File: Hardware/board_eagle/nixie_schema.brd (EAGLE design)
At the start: 150 x 170 mm, 103 parts, among them P1 100k, Q1 BC856B, Q2 IRF740S, U2 MC7940N

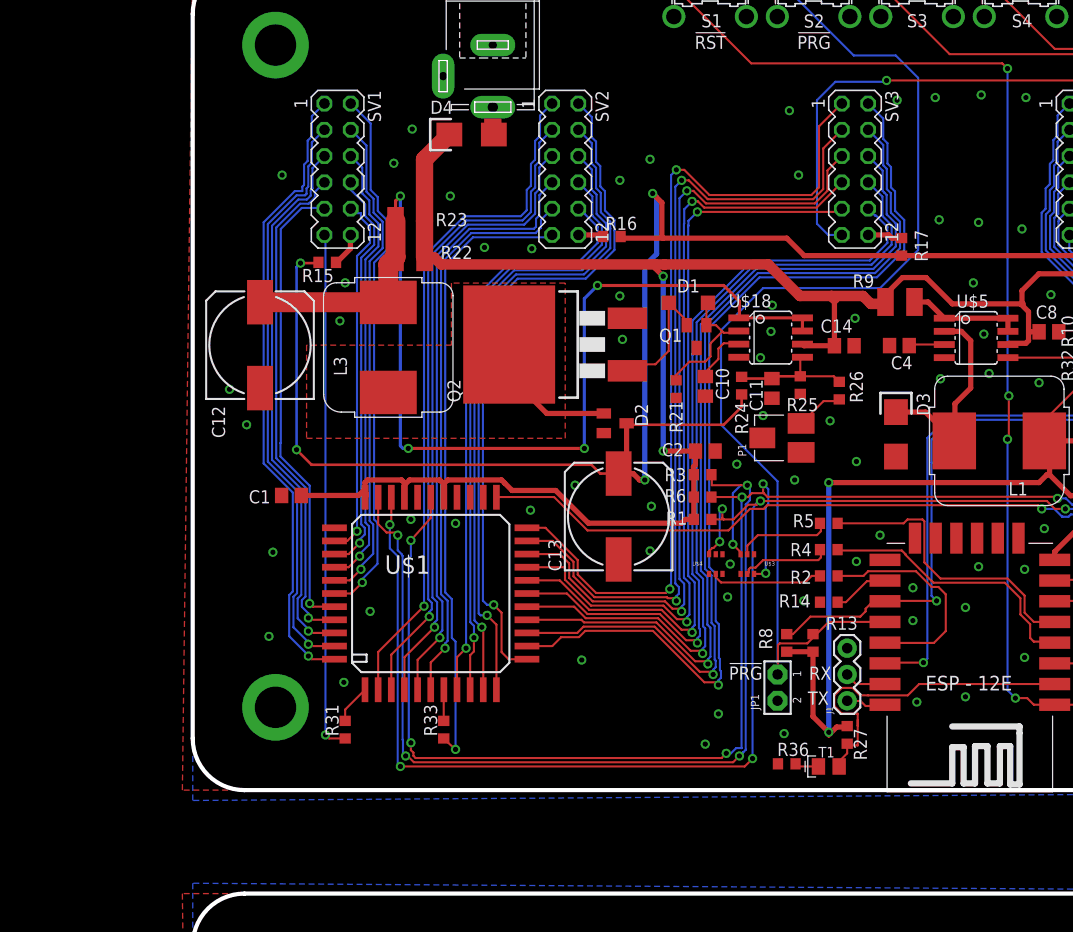
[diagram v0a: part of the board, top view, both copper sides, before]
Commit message: Modified both switching PSUs for the new VFD requirements
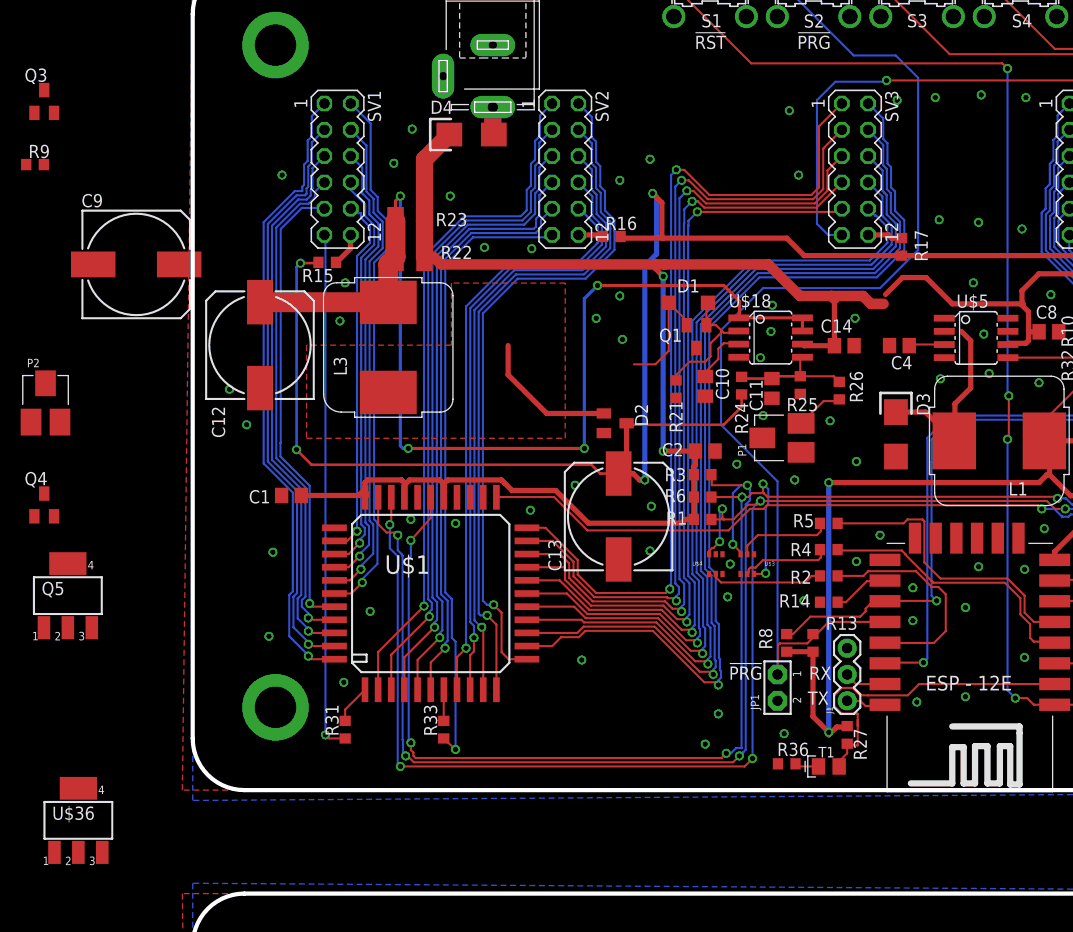
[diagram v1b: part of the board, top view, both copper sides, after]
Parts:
- removed Q2: IRF740S, nixe_cmp:D2PACK
- added C9: 220u, rcl:153CLV-1014
- added P2: 10k, nixe_cmp:UNI_POT_SMD
- added Q3: BC856B, nixe_cmp:SOT23
- added Q4: BCX70H, nixe_cmp:SOT23
- added Q5: NTF5P03, nixe_cmp:SOT223
- added U$36: IPN60R3K4CE_NMOS, nixe_cmp:SOT223
- R9: value 0.5R -> 1k; device eagle-ltspice:R1210 -> resistor:R0603
- moved R9 84.6 mm to (-15.2, 60.5)
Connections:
- new net N$102: Q3.2, Q4.2, Q5.1
- net +3V3: now also P2.P$1
- net GND: now also C9.-, Q3.3, U$36.3, U$5.2; no longer Q2.3
- net N$103: now also P2.P$2
- net N$13: now also Q5.2, Q5.4; no longer U$5.2
- net N$5: now also Q3.1, Q4.1; no longer U$5.7
- net N$95: now also U$36.1; no longer Q2.1
- net VCC: now also C9.+, Q4.3, Q5.3, U$5.7
- net V_PULSE: now also U$36.2, U$36.4; no longer Q2.2
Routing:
- net N$5: track 11.0 -> 0.00 mm
- net N$13: track 19.8 -> 18.2 mm
- net VCC: track 258.9 -> 257.9 mm
- net N$95: track 12.3 -> 11.4 mm

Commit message: Modified IN-14 device to accomodate IV-11 VFD
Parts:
- N1, N2, N3, N4, N5, N6: value IN-14_FIXED -> IN-14_IV-11_COMBI; device russian-nixies:IN-14 -> nixe_cmp:IN-14_IV-11
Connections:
- net N$1: now also N2.RHDP(NC); no longer N2.RHDP
- net N$10: now also N1.A(NC); no longer N1.A
- net N$19: now also N2.A(NC); no longer N2.A
- net N$2: now also N1.6(G); no longer N1.6
- net N$21: now also N3.A(NC); no longer N3.A
- net N$23: now also N2.6(G); no longer N2.6
- net N$24: now also N1.9(D); no longer N1.9
- net N$25: now also N1.1(GRID); no longer N1.1
- net N$26: now also N1.2(C); no longer N1.2
- net N$27: now also N1.3(DP); no longer N1.3
- net N$28: now also N1.4(B); no longer N1.4
- net N$29: now also N1.5(A); no longer N1.5
- net N$30: now also N1.RHDP(NC); no longer N1.RHDP
- net N$31: now also N2.7(F); no longer N2.7
- net N$32: now also N2.8(E); no longer N2.8
- net N$33: now also N2.9(D); no longer N2.9
- net N$34: now also N2.0(CAT); no longer N2.0
- net N$35: now also N3.RHDP(NC); no longer N3.RHDP
- net N$36: no longer N3.6
- net N$37: no longer N3.7
- net N$38: now also N2.5(A); no longer N2.5
- net N$39: now also N2.4(B); no longer N2.4
- net N$40: now also N2.3(DP); no longer N2.3
- net N$41: now also N2.2(C); no longer N2.2
- net N$42: now also N2.1(GRID); no longer N2.1
- net N$43: no longer N3.8
- net N$44: no longer N3.9
- net N$45: now also N6.A(NC); no longer N6.A
- net N$46: no longer N3.0
- net N$47: now also N4.RHDP(NC); no longer N4.RHDP
- net N$48: no longer N4.6
- net N$49: no longer N3.5
- net N$50: no longer N3.4
- net N$51: no longer N3.3
- net N$52: no longer N3.2
- net N$53: no longer N3.1
- net N$54: no longer N4.7
- net N$55: no longer N4.8
- net N$56: no longer N4.9
- net N$57: no longer N4.0
- net N$58: now also N5.RHDP(NC); no longer N5.RHDP
- net N$59: no longer N4.5
- net N$6: now also N1.7(F); no longer N1.7
- net N$60: no longer N4.4
- net N$61: no longer N4.3
- net N$62: no longer N4.2
- net N$63: no longer N4.1
- net N$64: no longer N5.6
- net N$65: no longer N5.7
- net N$66: no longer N5.8
- net N$67: no longer N5.9
- net N$68: no longer N5.0
- net N$69: no longer N5.5
- net N$7: now also N1.8(E); no longer N1.8
- net N$70: no longer N5.4
- net N$71: no longer N5.3
- net N$72: no longer N5.2
- net N$73: no longer N5.1
- net N$75: now also N6.RHDP(NC); no longer N6.RHDP
- net N$76: no longer N6.6
- net N$77: no longer N6.7
- net N$78: no longer N6.8
- net N$79: no longer N6.9
- net N$80: no longer N6.5
- net N$81: no longer N6.4
- net N$82: no longer N6.3
- net N$83: no longer N6.2
- net N$84: no longer N6.1
- net N$86: no longer N6.0
- net N$88: now also N4.A(NC); no longer N4.A
- net N$94: now also N1.0(CAT); no longer N1.0
- net N$98: now also N5.A(NC); no longer N5.A
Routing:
- net N$83: track 20.0 -> 6.89 mm
- net N$79: track 20.0 -> 6.89 mm
- net N$52: track 20.0 -> 6.89 mm
- net N$41: track 20.0 -> 6.89 mm
- net N$33: track 20.0 -> 6.89 mm
- net N$26: track 20.0 -> 6.89 mm
- net N$24: track 20.0 -> 6.89 mm
- net N$72: track 20.0 -> 6.89 mm
- net N$67: track 20.0 -> 6.89 mm
- net N$62: track 20.0 -> 6.89 mm
- net N$56: track 20.0 -> 6.89 mm
- net N$44: track 20.0 -> 6.89 mm
- net N$94: track 14.3 -> 5.37 mm
- net N$68: track 14.3 -> 5.37 mm
- net N$57: track 14.3 -> 5.37 mm
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
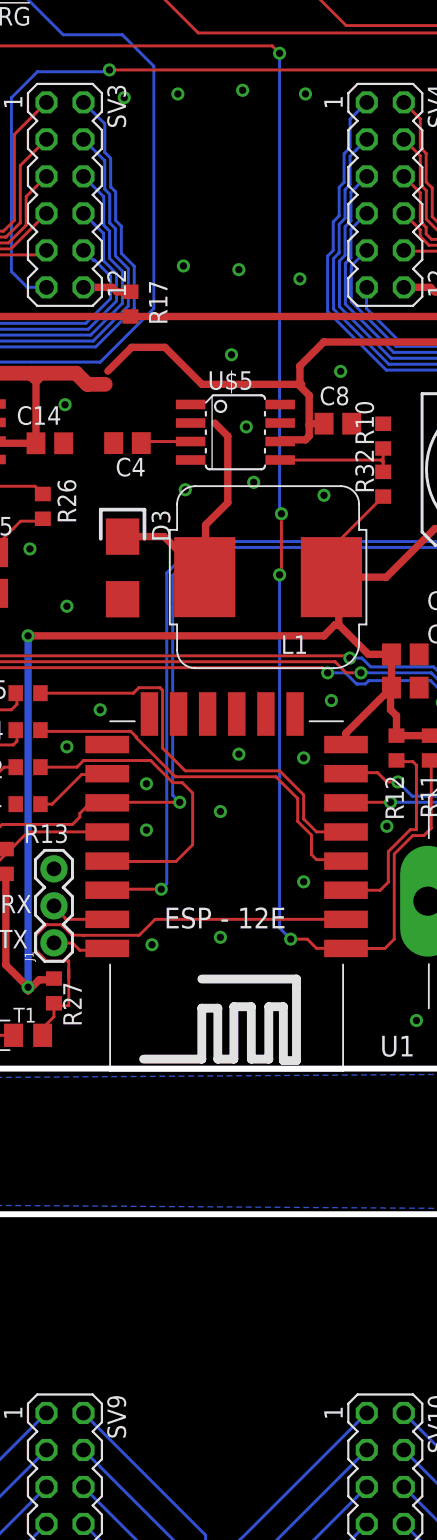
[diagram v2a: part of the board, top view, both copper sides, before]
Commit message: Added Eagle libraries for components. New symbols for Solder bridge and cut trace comps
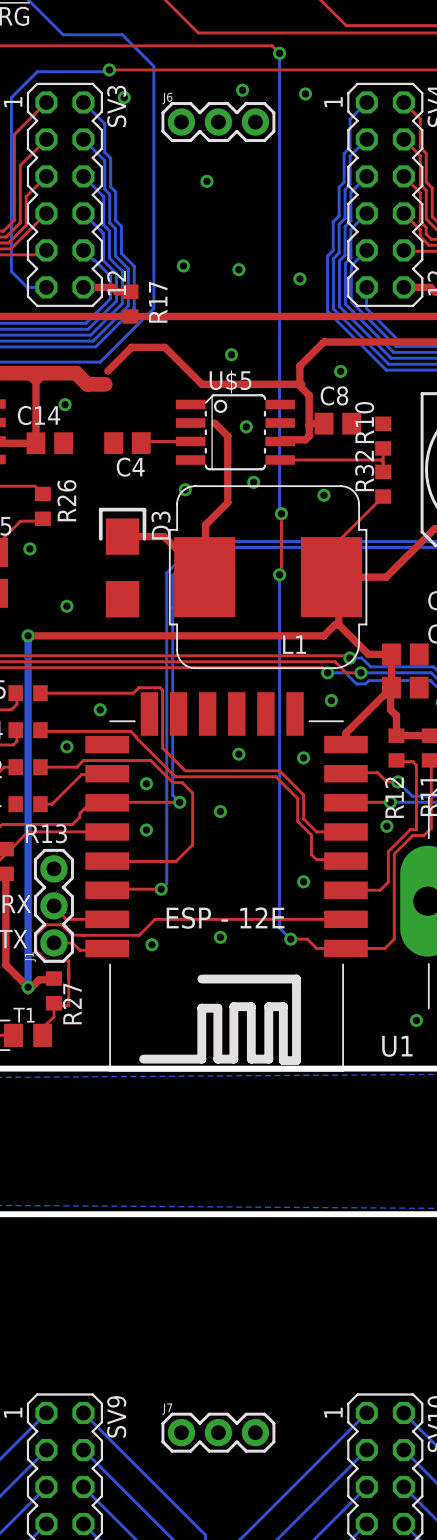
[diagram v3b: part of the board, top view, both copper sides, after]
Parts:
- added J6, J7: (no value), SparkFun-Connectors:1X03
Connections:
- net +3V3: now also J6.2, J7.2
- net GND: now also J6.3, J7.3
- net VCC: now also J6.1, J7.1
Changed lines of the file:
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@@
 <layer number="148" name="DrillLegend_01-20" color="7" fill="1" visible="no" active="yes"/>
 <layer number="149" name="DrillLegend_02-15" color="7" fill="1" visible="no" active="yes"/>
-<layer number="150" name="Notes" color="7" fill="1" visible="no" active="yes"/>
+<layer number="150" name="Notes" color="7" fill="1" visible="yes" active="yes"/>
 <layer number="151" name="HeatSink" color="7" fill="1" visible="no" active="yes"/>
 <layer number="152" name="_bDocu" color="7" fill="1" visible="no" active="yes"/>
@@
 <attribute name="V_DS" value="&gt;220 V" x="-11.049" y="-2.921" size="1.778" layer="27" display="off"/>
 </element>
-<element name="N1" library="nixe_cmp" package="IN-14_IV-11" value="IN-14_IV-11_COMBI" x="14" y="-50" rot="R180"/>
-<element name="N2" library="nixe_cmp" package="IN-14_IV-11" value="IN-14_IV-11_COMBI" x="36" y="-50" rot="R180"/>
-<element name="N3" library="nixe_cmp" package="IN-14_IV-11" value="IN-14_IV-11_COMBI" x="64" y="-50" rot="R180"/>
-<element name="N4" library="nixe_cmp" package="IN-14_IV-11" value="IN-14_IV-11_COMBI" x="86" y="-50" rot="R180"/>
-<element name="N5" library="nixe_cmp" package="IN-14_IV-11" value="IN-14_IV-11_COMBI" x="114" y="-50" rot="R180"/>
-<element name="N6" library="nixe_cmp" package="IN-14_IV-11" value="IN-14_IV-11_COMBI" x="136" y="-50" rot="R180"/>
+<element name="N1" library="nixe_cmp" package="IN-14_IV-11" value="IN-14_IV-11_COMBI" x="14" y="-50" locked="yes" rot="R180"/>
+<element name="N2" library="nixe_cmp" package="IN-14_IV-11" value="IN-14_IV-11_COMBI" x="36" y="-50" locked="yes" rot="R180"/>
+<element name="N3" library="nixe_cmp" package="IN-14_IV-11" value="IN-14_IV-11_COMBI" x="64" y="-50" locked="yes" rot="R180"/>
+<element name="N4" library="nixe_cmp" package="IN-14_IV-11" value="IN-14_IV-11_COMBI" x="86" y="-50" locked="yes" rot="R180"/>
+<element name="N5" library="nixe_cmp" package="IN-14_IV-11" value="IN-14_IV-11_COMBI" x="114" y="-50" locked="yes" rot="R180"/>
+<element name="N6" library="nixe_cmp" package="IN-14_IV-11" value="IN-14_IV-11_COMBI" x="136" y="-50" locked="yes" rot="R180"/>
+<element name="J6" library="SparkFun-Connectors" package="1X03" value="" x="72" y="65" locked="yes"/>
+<element name="J7" library="SparkFun-Connectors" package="1X03" value="" x="72" y="-25" locked="yes"/>
 </elements>
 <signals>
@@
 <contactref element="Q4" pad="3"/>
 <contactref element="Q5" pad="3"/>
-<wire x1="78.8964" y1="43.18" x2="78.7794" y2="44.333" width="0" layer="19" extent="1-1"/>
+<contactref element="J6" pad="1"/>
+<contactref element="J7" pad="1"/>
+<wire x1="70.866" y1="49.53" x2="72" y2="65" width="0" layer="19" extent="1-1"/>
 <wire x1="66.766" y1="46.99" x2="66.948" y2="47.898" width="0" layer="19" extent="1-1"/>
+<wire x1="78.7794" y1="44.333" x2="78.8964" y2="43.18" width="0" layer="19" extent="1-1"/>
 <wire x1="-1.311" y1="50.8" x2="22.4" y2="51.5" width="0" layer="19" extent="1-1"/>
 <wire x1="-16.09" y1="60.452" x2="-1.311" y2="50.8" width="0" layer="19" extent="1-1"/>
 <wire x1="-9.7536" y1="15.6972" x2="10.494" y2="28.474" width="0" layer="19" extent="1-1"/>
 <wire x1="-14.351" y1="28.659" x2="-9.7536" y2="15.6972" width="0" layer="19" extent="1-1"/>
+<wire x1="72" y1="-25" x2="48.426" y2="26.162" width="0" layer="19" extent="1-1"/>
 </signal>
 <signal name="GND">
@@
 <via x="75.946" y="54.864" extent="1-16" drill="0.5"/>
 <via x="76.2" y="67.183" extent="1-16" drill="0.5"/>
-<via x="71.755" y="66.929" extent="1-16" drill="0.5"/>
+<via x="73.755" y="60.929" extent="1-16" drill="0.5"/>
 <via x="80.137" y="54.229" extent="1-16" drill="0.5"/>
 <via x="80.518" y="66.929" extent="1-16" drill="0.5"/>
@@
 <contactref element="Q3" pad="3"/>
 <contactref element="U$36" pad="3"/>
+<contactref element="J6" pad="3"/>
+<contactref element="J7" pad="3"/>
 <wire x1="143.51" y1="53.848" x2="142" y2="72" width="0" layer="19" extent="1-1"/>
 <wire x1="145.669" y1="50.546" x2="143.51" y2="53.848" width="0" layer="19" extent="1-1"/>
@@
 <wire x1="72.136" y1="55.118" x2="75.946" y2="54.864" width="0" layer="19" extent="1-1"/>
 <wire x1="80.137" y1="54.229" x2="75.946" y2="54.864" width="0" layer="19" extent="1-1"/>
+<wire x1="73.755" y1="60.929" x2="72.136" y2="55.118" width="0" layer="19" extent="1-1"/>
+<wire x1="77.08" y1="65" x2="73.755" y2="60.929" width="0" layer="19" extent="1-1"/>
+<wire x1="76.2" y1="67.183" x2="77.08" y2="65" width="0" layer="19" extent="1-1"/>
+<wire x1="80.518" y1="66.929" x2="77.08" y2="65" width="0" layer="19" extent="1-1"/>
 <wire x1="103.378" y1="45.339" x2="96.393" y2="45.212" width="0" layer="19" extent="1-1"/>
 <wire x1="105.918" y1="45.298" x2="103.378" y2="45.339" width="0" layer="19" extent="1-1"/>
@@
 <wire x1="6.5" y1="38.85" x2="5.207" y2="35.306" width="0" layer="19" extent="1-1"/>
 <wire x1="3.556" y1="38.735" x2="6.5" y2="38.85" width="0" layer="19" extent="1-1"/>
+<wire x1="68.072" y1="66.675" x2="73.755" y2="60.929" width="0" layer="19" extent="1-1"/>
 <wire x1="7.366" y1="14.859" x2="7.747" y2="22.987" width="0" layer="19" extent="1-1"/>
 <wire x1="8" y1="8" x2="7.366" y2="14.859" width="0" layer="19" extent="1-1"/>
@@
 <wire x1="14.732" y1="49.022" x2="14.224" y2="45.339" width="0" layer="19" extent="1-1"/>
 <wire x1="118.491" y1="62.611" x2="108.585" y2="60.579" width="0" layer="19" extent="1-1"/>
+<wire x1="90.678" y1="66.294" x2="80.518" y2="66.929" width="0" layer="19" extent="1-1"/>
 <wire x1="37.592" y1="12.573" x2="41.16" y2="22.29" width="0" layer="19" extent="1-1"/>
+<wire x1="82.2606" y1="77.2446" x2="80.518" y2="66.929" width="0" layer="19" extent="1-1"/>
+<wire x1="92.2606" y1="77.2446" x2="82.2606" y2="77.2446" width="0" layer="19" extent="1-1"/>
+<wire x1="102.2606" y1="77.2446" x2="92.2606" y2="77.2446" width="0" layer="19" extent="1-1"/>
+<wire x1="72.2606" y1="77.2446" x2="82.2606" y2="77.2446" width="0" layer="19" extent="1-1"/>
+<wire x1="62.2606" y1="77.2446" x2="72.2606" y2="77.2446" width="0" layer="19" extent="1-1"/>
+<wire x1="52.2606" y1="77.2446" x2="62.2606" y2="77.2446" width="0" layer="19" extent="1-1"/>
+<wire x1="57.658" y1="65.659" x2="68.072" y2="66.675" width="0" layer="19" extent="1-1"/>
+<wire x1="58.547" y1="59.436" x2="57.658" y2="65.659" width="0" layer="19" extent="1-1"/>
 <wire x1="41.275" y1="58.928" x2="32.766" y2="52.324" width="0" layer="19" extent="1-1"/>
 <wire x1="44.196" y1="60.96" x2="41.275" y2="58.928" width="0" layer="19" extent="1-1"/>
@@
 <wire x1="135.255" y1="10.795" x2="135.763" y2="3.937" width="0" layer="19" extent="1-1"/>
 <wire x1="142" y1="8" x2="135.255" y2="10.795" width="0" layer="19" extent="1-1"/>
-<wire x1="71.755" y1="66.929" x2="72.136" y2="55.118" width="0" layer="19" extent="1-1"/>
-<wire x1="68.072" y1="66.675" x2="71.755" y2="66.929" width="0" layer="19" extent="1-1"/>
-<wire x1="76.2" y1="67.183" x2="71.755" y2="66.929" width="0" layer="19" extent="1-1"/>
-<wire x1="80.518" y1="66.929" x2="76.2" y2="67.183" width="0" layer="19" extent="1-1"/>
-<wire x1="90.678" y1="66.294" x2="80.518" y2="66.929" width="0" layer="19" extent="1-1"/>
-<wire x1="72.2606" y1="77.2446" x2="71.755" y2="66.929" width="0" layer="19" extent="1-1"/>
-<wire x1="82.2606" y1="77.2446" x2="72.2606" y2="77.2446" width="0" layer="19" extent="1-1"/>
-<wire x1="92.2606" y1="77.2446" x2="82.2606" y2="77.2446" width="0" layer="19" extent="1-1"/>
-<wire x1="102.2606" y1="77.2446" x2="92.2606" y2="77.2446" width="0" layer="19" extent="1-1"/>
-<wire x1="62.2606" y1="77.2446" x2="72.2606" y2="77.2446" width="0" layer="19" extent="1-1"/>
-<wire x1="52.2606" y1="77.2446" x2="62.2606" y2="77.2446" width="0" layer="19" extent="1-1"/>
-<wire x1="57.658" y1="65.659" x2="68.072" y2="66.675" width="0" layer="19" extent="1-1"/>
-<wire x1="58.547" y1="59.436" x2="57.658" y2="65.659" width="0" layer="19" extent="1-1"/>
 <wire x1="88.138" y1="3.302" x2="80.391" y2="12.827" width="0" layer="19" extent="1-1"/>
 <wire x1="8" y1="72" x2="8.636" y2="59.436" width="0" layer="19" extent="1-1"/>
@@
 <wire x1="8" y1="-18" x2="-8.7376" y2="-6.0198" width="0" layer="19" extent="1-1"/>
 <wire x1="142" y1="-18" x2="135.763" y2="3.937" width="0" layer="19" extent="1-1"/>
+<wire x1="77.08" y1="-25" x2="88.138" y2="3.302" width="0" layer="19" extent="1-1"/>
 <wire x1="8" y1="-82" x2="8" y2="-18" width="0" layer="19" extent="1-1"/>
 <wire x1="142" y1="-82" x2="142" y2="-18" width="0" layer="19" extent="1-1"/>
@@
 <wire x1="146.05" y1="52.998" x2="147.67" y2="54.618" width="0.508" layer="1"/>
 <contactref element="P2" pad="P$1"/>
+<contactref element="J6" pad="2"/>
+<contactref element="J7" pad="2"/>
+<wire x1="85.852" y1="39.282" x2="74.54" y2="65" width="0" layer="19" extent="1-1"/>
+<wire x1="74.54" y1="-25" x2="61.468" y2="5.334" width="0" layer="19" extent="1-1"/>
 <wire x1="-15.624" y1="35.565" x2="57.404" y2="13.374" width="0" layer="19" extent="1-1"/>
 </signal>
